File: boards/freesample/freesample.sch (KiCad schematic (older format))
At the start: 2 parts

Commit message: Continued initial schematic capture
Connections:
- net labels added: 3V3_N, COARSE_EN, COARSE_SCLK, COARSE_SDIN, COARSE_SLOAD, DAC_CLR_N, DAC_CS_N, DAC_MISO, DAC_MOSI, DAC_MUXOUT, DAC_SCK, FINE_SEL0_N, FINE_SEL0_P, FINE_SEL1_N, FINE_SEL1_P, FINE_SEL2_N, FINE_SEL2_P, FINE_SEL3_N, FINE_SEL3_P, FINE_SEL4_N, FINE_SEL4_P, LDAC_N, OSC_FS0, OSC_FS1, OSC_OE, OSC_OS, OSC_PWR_EN, PLL_CLK, PLL_CLKIN0, PLL_CLKIN1, PLL_DATA, PLL_HOLDOVER, PLL_LD, PLL_LE, PLL_SYNC, RANGE_SEL, SAMP_MUXSEL0, SAMP_MUXSEL1, SERDES_MDC, SERDES_MDIO, SERDES_MODE_SEL, SERDES_RST_N
- wire segments 70 -> 138
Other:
- note added: "Analog sensors"
- note added: "CML to FPGA\nNeed converter to LVDS"
- note added: "LVCMOS18"
- note added: "LVCMOS33"
- note added: "LVDS from FPGA"
- note added: "LVDS from FPGA\nNeed converter to CML"
- note added: "TBD"

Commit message: Continued work on schematic capture
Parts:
- added F1: TBD, symbol power-azonenberg:FUSE_PWROUT
- added FB1: TBD, symbol passive-azonenberg:INDUCTOR_PWROUT
- added J2: CONN_3_PWROUT, symbol power-azonenberg:CONN_3_PWROUT
- J1: renamed from J?; symbol conn:CONN_COAXIAL -> freesample-rescue:CONN_COAXIAL-conn
- gave numbers to parts that had none: 1
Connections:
- net labels added: 12V0, 12V0_RAW
- wire segments 138 -> 149
- no-connect marks 0 -> 1
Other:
- note removed: "TBD"
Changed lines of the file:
@@
 $EndSheet
 $Comp
-L conn:CONN_COAXIAL J?
+L freesample-rescue:CONN_COAXIAL-conn J1
 U 1 1 5C201EC1
 P 750 850
-F 0 "J?" H 703 1088 50  0000 C CNN
+F 0 "J1" H 703 1088 50  0000 C CNN
 F 1 "SMA" H 703 997 50  0000 C CNN
 F 2 "" H 750 850 50  0001 C CNN
@@
 VIN
 $Comp
-L analog-azonenberg:SPLITTER_SUSUMU_PS R?
+L analog-azonenberg:SPLITTER_SUSUMU_PS R1
 U 1 1 5C20338C
 P 1350 1000
-F 0 "R?" H 1600 1375 50  0000 C CNN
+F 0 "R1" H 1600 1375 50  0000 C CNN
 F 1 "PS3216GT2-R50-T1‎" H 1600 1284 50  0000 C CNN
 F 2 "" H 1350 1000 50  0001 C CNN
@@
 Text Label 7400 1500 0    50   ~ 0
 OSC_FS0
-Text Label 5850 5500 0    50   ~ 0
+Text Label 2350 7500 0    50   ~ 0
 OSC_PWR_EN
 Text Label 2350 5600 0    50   ~ 0
@@
 Text Notes 3650 5400 0    50   ~ 0
 LVCMOS18
-Text Notes 5850 5400 0    50   ~ 0
-TBD
 Text Notes 3650 6800 0    50   ~ 0
 LVDS from FPGA\nNeed converter to CML
+Text Label 1800 2000 0    50   ~ 0
+5V0
+Wire Wire Line
+	1800 2000 1700 2000
+Text Label 1800 2100 0    50   ~ 0
+3V3
+Wire Wire Line
+	1800 2100 1700 2100
+Text Label 1800 2200 0    50   ~ 0
+1V8
+Wire Wire Line
+	1800 2200 1700 2200
+Text Label 1800 2300 0    50   ~ 0
+1V0
+Wire Wire Line
+	1800 2300 1700 2300
+Text Label 1800 2400 0    50   ~ 0
+3V0_N
+Wire Wire Line
+	1800 2400 1700 2400
+Text Label 1800 2500 0    50   ~ 0
+3V3_N
+Wire Wire Line
+	1800 2500 1700 2500
+Text Label 1800 2600 0    50   ~ 0
+5V0_N
+Wire Wire Line
+	1800 2600 1700 2600
+Text Label 750  2000 2    50   ~ 0
+12V0
+Wire Wire Line
+	750  2000 850  2000
+Text Label 750  2100 2    50   ~ 0
+GND
+Wire Wire Line
+	750  2100 850  2100
+NoConn ~ 13100 1000
+Text Label 13200 900  0    50   ~ 0
+GND
+Wire Wire Line
+	13200 900  13100 900
+Text Label 13200 800  0    50   ~ 0
+12V0_RAW
+Wire Wire Line
+	13100 800  13700 800
+$Comp
+L power-azonenberg:FUSE_PWROUT F1
+U 1 1 5C7169D1
+P 13950 800
+F 0 "F1" H 13950 1040 50  0000 C CNN
+F 1 "TBD" H 13950 949 50  0000 C CNN
+F 2 "" H 13950 800 60  0000 C CNN
+F 3 "" H 13950 800 60  0000 C CNN
+	1    13950 800
+	1    0    0    -1
+$EndComp
+$Comp
+L power-azonenberg:CONN_3_PWROUT J2
+U 1 1 5C717AA0
+P 12750 900
+F 0 "J2" H 12617 1200 50  0000 C CNN
+F 1 "CONN_3_PWROUT" H 12617 1116 40  0000 C CNN
+F 2 "" H 12750 900 60  0000 C CNN
+F 3 "" H 12750 900 60  0000 C CNN
+	1    12750 900
+	-1   0    0    -1
+$EndComp
+$Comp
+L passive-azonenberg:INDUCTOR_PWROUT FB1
+U 1 1 5C71964A
+P 14500 800
+F 0 "FB1" V 14342 800 40  0000 C CNN
+F 1 "TBD" V 14418 800 40  0000 C CNN
+F 2 "" H 14500 800 60  0000 C CNN
+F 3 "" H 14500 800 60  0000 C CNN
+	1    14500 800
+	0    1    1    0
+$EndComp
+Text Label 14800 800  0    50   ~ 0
+12V0
 $EndSCHEMATC

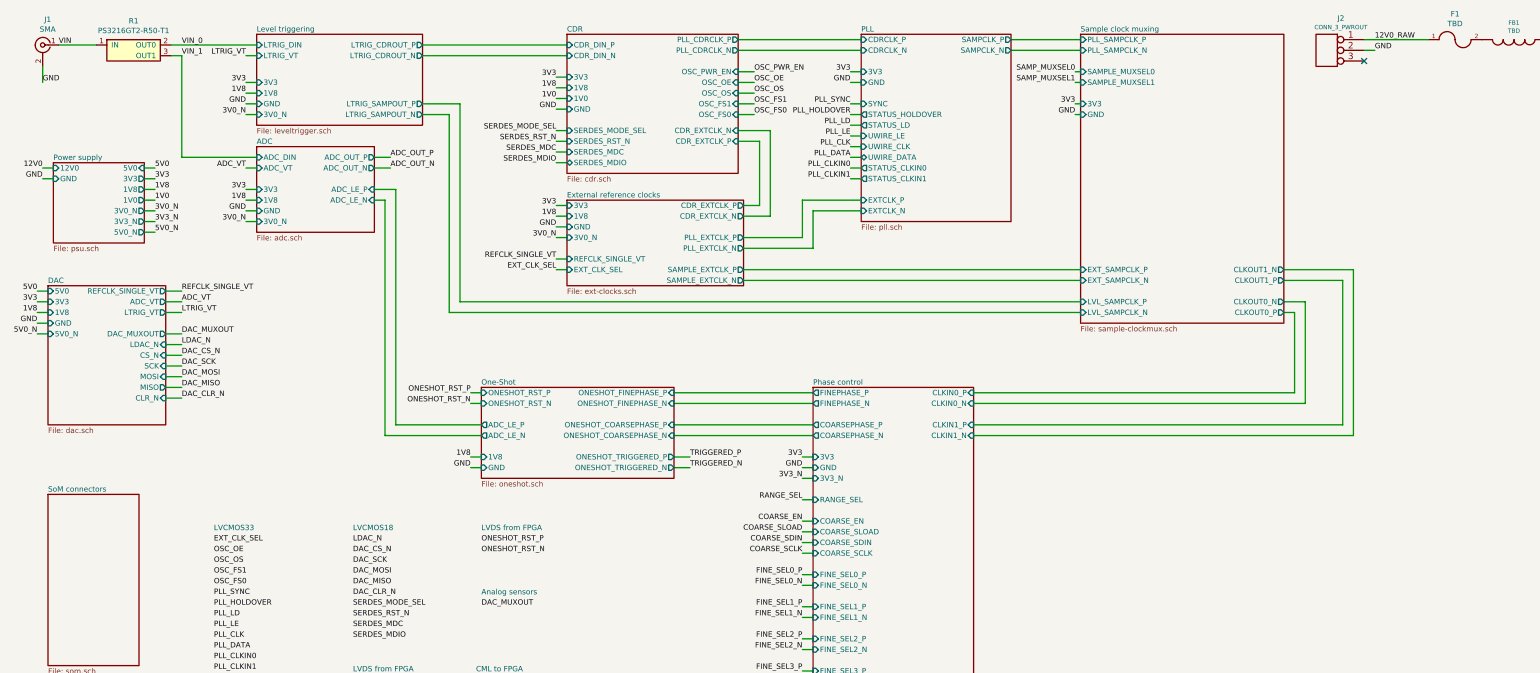
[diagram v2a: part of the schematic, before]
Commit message: Continued work on FREESAMPLE schematic including PSU.
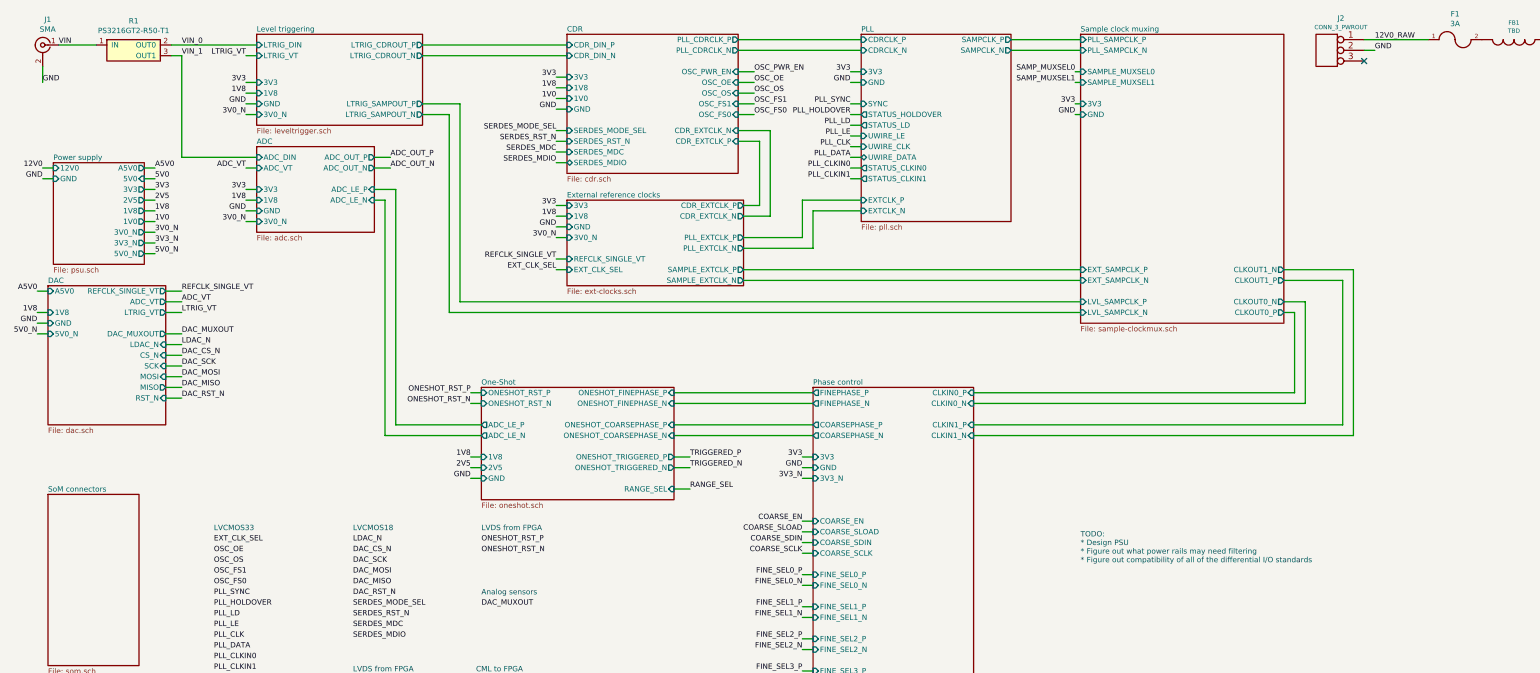
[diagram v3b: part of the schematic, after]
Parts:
- F1: value TBD -> 3A
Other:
- note added: "TODO:\n* Design PSU\n* Figure out what power rails may need filtering\n* Figure out compatibility of all of the differential I/O standards"
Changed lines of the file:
@@
 Sheet 1 12
 Title "FREESAMPLE Oscilloscope"
-Date "2018-12-17"
+Date "2019-02-23"
 Rev "0.1"
 Comp "Andrew D. Zonenberg / Antikernel Labs"
@@
 F3 "REFCLK_SINGLE_VT" O R 1900 3150 50
 F4 "ADC_VT" O R 1900 3250 50
-F5 "5V0" I L 800 3150 50
-F6 "5V0_N" I L 800 3550 50
-F7 "GND" I L 800 3450 50
-F8 "3V3" I L 800 3250 50
-F9 "DAC_MUXOUT" O R 1900 3550 50
-F10 "LDAC_N" I R 1900 3650 50
-F11 "CS_N" I R 1900 3750 50
-F12 "SCK" I R 1900 3850 50
-F13 "MOSI" I R 1900 3950 50
-F14 "MISO" O R 1900 4050 50
-F15 "CLR_N" I R 1900 4150 50
-F16 "1V8" I L 800 3350 50
+F5 "5V0_N" I L 800 3550 50
+F6 "GND" I L 800 3450 50
+F7 "DAC_MUXOUT" O R 1900 3550 50
+F8 "LDAC_N" I R 1900 3650 50
+F9 "CS_N" I R 1900 3750 50
+F10 "SCK" I R 1900 3850 50
+F11 "MOSI" I R 1900 3950 50
+F12 "MISO" O R 1900 4050 50
+F13 "1V8" I L 800 3350 50
+F14 "RST_N" I R 1900 4150 50
+F15 "A5V0" I L 800 3150 50
 $EndSheet
 $Sheet
@@
 $EndSheet
 $Sheet
-S 4850 4050 1800 850
+S 4850 4050 1800 1050
 U 5C15809A
 F0 "One-Shot" 50
@@
 F5 "ONESHOT_RST_N" I L 4850 4200 50
 F6 "1V8" I L 4850 4700 50
-F7 "GND" I L 4850 4800 50
+F7 "GND" I L 4850 4900 50
 F8 "ONESHOT_TRIGGERED_P" O R 6650 4700 50
 F9 "ONESHOT_TRIGGERED_N" O R 6650 4800 50
@@
 F12 "ONESHOT_COARSEPHASE_P" I R 6650 4400 50
 F13 "ONESHOT_COARSEPHASE_N" I R 6650 4500 50
+F14 "RANGE_SEL" I R 6650 5000 50
+F15 "2V5" I L 4850 4800 50
 $EndSheet
 $Comp
@@
 $EndSheet
 $Sheet
-S 850  1950 850  750
+S 850  1950 850  950
 U 5C204CCA
 F0 "Power supply" 50
 F1 "psu.sch" 50
-F2 "5V0" I R 1700 2000 50
-F3 "3V3" O R 1700 2100 50
-F4 "3V0_N" O R 1700 2400 50
-F5 "1V8" O R 1700 2200 50
+F2 "5V0" I R 1700 2100 50
+F3 "3V3" O R 1700 2200 50
+F4 "3V0_N" O R 1700 2600 50
+F5 "1V8" O R 1700 2400 50
 F6 "GND" I L 850 2100 50
-F7 "1V0" O R 1700 2300 50
-F8 "5V0_N" O R 1700 2600 50
+F7 "1V0" O R 1700 2500 50
+F8 "5V0_N" O R 1700 2800 50
 F9 "12V0" I L 850 2000 50
-F10 "3V3_N" O R 1700 2500 50
+F10 "3V3_N" O R 1700 2700 50
+F11 "2V5" O R 1700 2300 50
+F12 "A5V0" O R 1700 2000 50
 $EndSheet
 Text Label 8300 1100 2    50   ~ 0
@@
 	2050 3350 1900 3350
 Text Label 700  3150 2    50   ~ 0
-5V0
+A5V0
 Wire Wire Line
 	700  3150 800  3150
-Text Label 700  3250 2    50   ~ 0
-3V3
-Wire Wire Line
-	700  3250 800  3250
 Text Label 700  3450 2    50   ~ 0
 GND
@@
 Wire Wire Line
 	4750 4700 4850 4700
-Text Label 4750 4800 2    50   ~ 0
-GND
-Wire Wire Line
-	4750 4800 4850 4800
 Text Label 6800 4700 0    50   ~ 0
 TRIGGERED_P
@@
 DAC_MISO
 Text Label 3650 6000 0    50   ~ 0
-DAC_CLR_N
+DAC_RST_N
 Text Label 2050 3550 0    50   ~ 0
 DAC_MUXOUT
@@
 DAC_MISO
 Text Label 2050 4150 0    50   ~ 0
-DAC_CLR_N
+DAC_RST_N
 Wire Wire Line
 	2050 3550 1900 3550
@@
 F10 "3V3" I L 7950 4700 50
 F11 "GND" I L 7950 4800 50
-F12 "RANGE_SEL" I L 7950 5100 50
 F13 "COARSE_EN" I L 7950 5300 50
 F14 "COARSE_SLOAD" I L 7950 5400 50
@@
 Wire Wire Line
 	7850 4900 7950 4900
-Text Label 7850 5100 2    50   ~ 0
-RANGE_SEL
-Wire Wire Line
-	7850 5100 7950 5100
 Text Label 7850 5300 2    50   ~ 0
 COARSE_EN
@@
 Text Notes 3650 6800 0    50   ~ 0
 LVDS from FPGA\nNeed converter to CML
-Text Label 1800 2000 0    50   ~ 0
+Text Label 1800 2100 0    50   ~ 0
 5V0
-Wire Wire Line
-	1800 2000 1700 2000
-Text Label 1800 2100 0    50   ~ 0
-3V3
 Wire Wire Line
 	1800 2100 1700 2100
 Text Label 1800 2200 0    50   ~ 0
+3V3
+Wire Wire Line
+	1800 2200 1700 2200
+Text Label 1800 2400 0    50   ~ 0
 1V8
-Wire Wire Line
-	1800 2200 1700 2200
-Text Label 1800 2300 0    50   ~ 0
-1V0
-Wire Wire Line
-	1800 2300 1700 2300
-Text Label 1800 2400 0    50   ~ 0
-3V0_N
 Wire Wire Line
 	1800 2400 1700 2400
 Text Label 1800 2500 0    50   ~ 0
-3V3_N
+1V0
 Wire Wire Line
 	1800 2500 1700 2500
 Text Label 1800 2600 0    50   ~ 0
+3V0_N
+Wire Wire Line
+	1800 2600 1700 2600
+Text Label 1800 2700 0    50   ~ 0
+3V3_N
+Wire Wire Line
+	1800 2700 1700 2700
+Text Label 1800 2800 0    50   ~ 0
 5V0_N
 Wire Wire Line
-	1800 2600 1700 2600
+	1800 2800 1700 2800
 Text Label 750  2000 2    50   ~ 0
 12V0
@@
 P 13950 800
 F 0 "F1" H 13950 1040 50  0000 C CNN
-F 1 "TBD" H 13950 949 50  0000 C CNN
+F 1 "3A" H 13950 949 50  0000 C CNN
 F 2 "" H 13950 800 60  0000 C CNN
 F 3 "" H 13950 800 60  0000 C CNN
@@
 Text Label 14800 800  0    50   ~ 0
 12V0
+Text Label 6800 5000 0    50   ~ 0
+RANGE_SEL
+Wire Wire Line
+	6800 5000 6650 5000
+Wire Wire Line
+	4750 4900 4850 4900
+Text Label 4750 4900 2    50   ~ 0
+GND
+Text Label 4750 4800 2    50   ~ 0
+2V5
+Wire Wire Line
+	4750 4800 4850 4800
+Text Label 1800 2300 0    50   ~ 0
+2V5
+Wire Wire Line
+	1800 2300 1700 2300
+Text Notes 10450 5700 0    50   ~ 0
+TODO:\n* Design PSU\n* Figure out what power rails may need filtering\n* Figure out compatibility of all of the differential I/O standards
+Text Label 1800 2000 0    50   ~ 0
+A5V0
+Wire Wire Line
+	1800 2000 1700 2000
 $EndSCHEMATC
